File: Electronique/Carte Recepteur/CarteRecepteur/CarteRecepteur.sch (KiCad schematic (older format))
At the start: 1 part

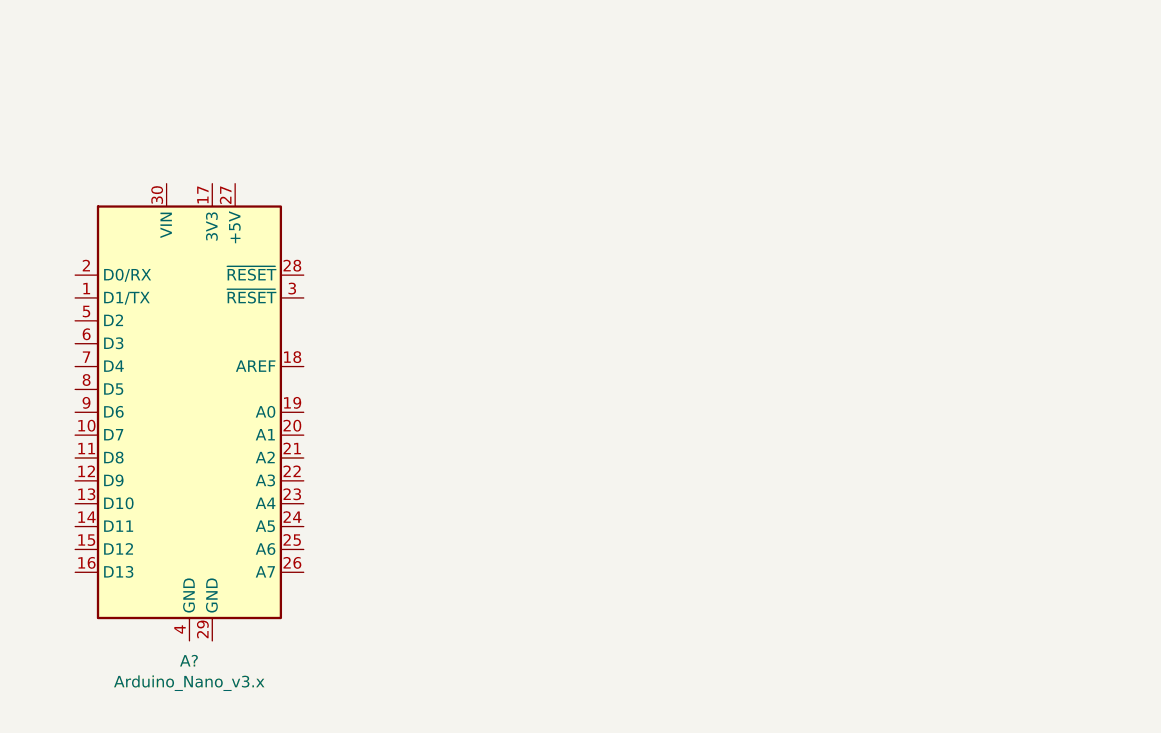
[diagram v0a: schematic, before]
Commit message: ajout trous vis bloc moteurs chassis
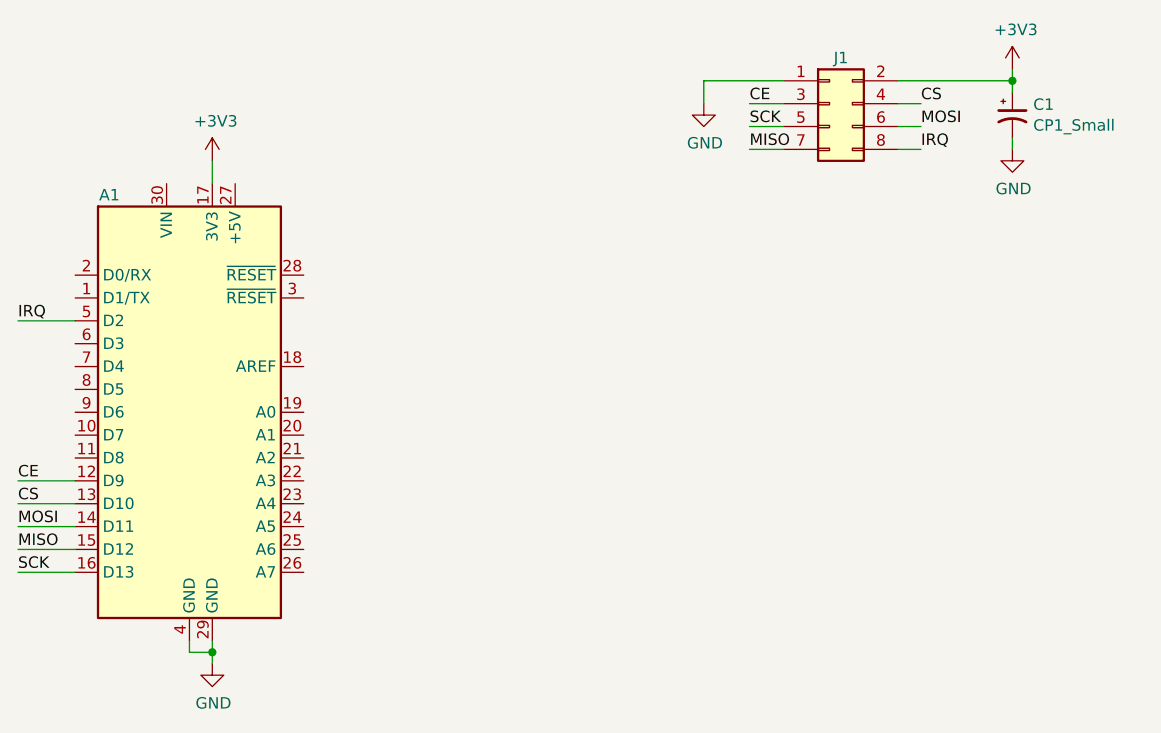
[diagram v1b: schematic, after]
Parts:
- added C1: CP1_Small, Capacitor_THT:CP_Radial_D5.0mm_P2.50mm, symbol Device:CP1_Small
- added J1: Conn_02x04_Odd_Even_MountingPin, Connector_PinHeader_2.54mm:PinHeader_2x04_P2.54mm_Vertical, symbol Connector_Generic:Conn_02x04_Odd_Even
- gave numbers to parts that had none: 1
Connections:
- net CE: now reaches A1.12 (D9)
- net CE: now also J1.3 (Pin_3)
- net CS: now reaches A1.13 (D10)
- net CS: now also J1.4 (Pin_4)
- net MOSI: now reaches A1.14 (D11)
- net MOSI: now also J1.6 (Pin_6)
- net MISO: now reaches A1.15 (D12)
- net MISO: now also J1.7 (Pin_7)
- net SCK: now reaches A1.16 (D13)
- net SCK: now also J1.5 (Pin_5)
- net +3V3: now reaches A1.17 (3V3)
- net +3V3: now also C1.1, J1.2 (Pin_2)
- net GND: now reaches A1.29 (GND)
- net GND: now also A1.4 (GND), C1.2, J1.1 (Pin_1)
- net IRQ: now reaches A1.5 (D2)
- net IRQ: now also J1.8 (Pin_8)
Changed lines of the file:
@@
 $EndDescr
 $Comp
-L MCU_Module:Arduino_Nano_v3.x A?
+L MCU_Module:Arduino_Nano_v3.x A1
 U 1 1 61373980
 P 4050 3000
-F 0 "A?" H 4050 1911 50  0000 C CNN
-F 1 "Arduino_Nano_v3.x" H 4050 1820 50  0000 C CNN
+F 0 "A1" H 3700 3950 50  0000 C CNN
+F 1 "Arduino_Nano_v3.x" H 4050 1820 50  0001 C CNN
 F 2 "Module:Arduino_Nano" H 4050 3000 50  0001 C CIN
 F 3 "http://www.mouser.com/pdfdocs/Gravitech_Arduino_Nano3_0.pdf" H 4050 3000 50  0001 C CNN
@@
 	1    0    0    -1
 $EndComp
+$Comp
+L Connector_Generic:Conn_02x04_Odd_Even J1
+U 1 1 613798DD
+P 6850 1650
+F 0 "J1" H 6900 1850 50  0000 C CNN
+F 1 "Conn_02x04_Odd_Even_MountingPin" H 6900 1300 50  0001 C CNN
+F 2 "Connector_PinHeader_2.54mm:PinHeader_2x04_P2.54mm_Vertical" H 6850 1650 50  0001 C CNN
+F 3 "~" H 6850 1650 50  0001 C CNN
+	1    6850 1650
+	1    0    0    -1
+$EndComp
+$Comp
+L power:+3V3 #PWR0101
+U 1 1 6137ADBA
+P 4150 1900
+F 0 "#PWR0101" H 4150 1750 50  0001 C CNN
+F 1 "+3V3" H 4165 2073 50  0000 C CNN
+F 2 "" H 4150 1900 50  0001 C CNN
+F 3 "" H 4150 1900 50  0001 C CNN
+	1    4150 1900
+	1    0    0    -1
+$EndComp
+Wire Wire Line
+	4150 2000 4150 1900
+$Comp
+L power:+3V3 #PWR0102
+U 1 1 6137B938
+P 7650 1500
+F 0 "#PWR0102" H 7650 1350 50  0001 C CNN
+F 1 "+3V3" H 7665 1673 50  0000 C CNN
+F 2 "" H 7650 1500 50  0001 C CNN
+F 3 "" H 7650 1500 50  0001 C CNN
+	1    7650 1500
+	1    0    0    -1
+$EndComp
+Wire Wire Line
+	7650 1550 7650 1500
+$Comp
+L Device:CP1_Small C1
+U 1 1 6137E190
+P 7650 1700
+F 0 "C1" H 7741 1746 50  0000 L CNN
+F 1 "CP1_Small" H 7741 1655 50  0000 L CNN
+F 2 "Capacitor_THT:CP_Radial_D5.0mm_P2.50mm" H 7650 1700 50  0001 C CNN
+F 3 "~" H 7650 1700 50  0001 C CNN
+	1    7650 1700
+	1    0    0    -1
+$EndComp
+Wire Wire Line
+	7650 1600 7650 1550
+Connection ~ 7650 1550
+$Comp
+L power:GND #PWR0103
+U 1 1 6137E9C8
+P 7650 1850
+F 0 "#PWR0103" H 7650 1600 50  0001 C CNN
+F 1 "GND" H 7655 1677 50  0000 C CNN
+F 2 "" H 7650 1850 50  0001 C CNN
+F 3 "" H 7650 1850 50  0001 C CNN
+	1    7650 1850
+	1    0    0    -1
+$EndComp
+Wire Wire Line
+	7650 1800 7650 1850
+$Comp
+L power:GND #PWR0104
+U 1 1 6137F4C9
+P 4150 4100
+F 0 "#PWR0104" H 4150 3850 50  0001 C CNN
+F 1 "GND" H 4155 3927 50  0000 C CNN
+F 2 "" H 4150 4100 50  0001 C CNN
+F 3 "" H 4150 4100 50  0001 C CNN
+	1    4150 4100
+	1    0    0    -1
+$EndComp
+Wire Wire Line
+	4150 4100 4150 4050
+Wire Wire Line
+	4150 4050 4050 4050
+Wire Wire Line
+	4050 4050 4050 4000
+Connection ~ 4150 4050
+Wire Wire Line
+	4150 4050 4150 4000
+Wire Wire Line
+	7150 1550 7650 1550
+Wire Wire Line
+	7150 1650 7250 1650
+Wire Wire Line
+	7150 1750 7250 1750
+Wire Wire Line
+	7150 1850 7250 1850
+Text Label 7250 1650 0    50   ~ 0
+CS
+Text Label 7250 1750 0    50   ~ 0
+MOSI
+Text Label 7250 1850 0    50   ~ 0
+IRQ
+Text Label 6500 1650 0    50   ~ 0
+CE
+Text Label 6500 1750 0    50   ~ 0
+SCK
+Text Label 6500 1850 0    50   ~ 0
+MISO
+$Comp
+L power:GND #PWR0105
+U 1 1 61381943
+P 6300 1650
+F 0 "#PWR0105" H 6300 1400 50  0001 C CNN
+F 1 "GND" H 6305 1477 50  0000 C CNN
+F 2 "" H 6300 1650 50  0001 C CNN
+F 3 "" H 6300 1650 50  0001 C CNN
+	1    6300 1650
+	1    0    0    -1
+$EndComp
+Wire Wire Line
+	6300 1550 6300 1650
+Wire Wire Line
+	6300 1550 6650 1550
+Wire Wire Line
+	6500 1650 6650 1650
+Wire Wire Line
+	6500 1750 6650 1750
+Wire Wire Line
+	6500 1850 6650 1850
+Wire Wire Line
+	3300 3700 3550 3700
+Text Label 3300 3700 0    50   ~ 0
+SCK
+Wire Wire Line
+	3550 3600 3300 3600
+Wire Wire Line
+	3550 3500 3300 3500
+Wire Wire Line
+	3550 3400 3300 3400
+Text Label 3300 3600 0    50   ~ 0
+MISO
+Text Label 3300 3500 0    50   ~ 0
+MOSI
+Text Label 3300 3400 0    50   ~ 0
+CS
+Wire Wire Line
+	3550 3300 3300 3300
+Text Label 3300 3300 0    50   ~ 0
+CE
+Text Label 3300 2600 0    50   ~ 0
+IRQ
+Wire Wire Line
+	3300 2600 3550 2600
 $EndSCHEMATC

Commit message: pcb recepteur
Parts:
- added H1, H2: MountingHole, MountingHole:MountingHole_2.2mm_M2_ISO7380_Pad, symbol Mechanical:MountingHole
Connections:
- net CE: now also A1.23 (A4); no longer A1.12 (D9)
- net IRQ: no longer A1.5 (D2)
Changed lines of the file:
@@
 $EndDescr
-$Comp
-L MCU_Module:Arduino_Nano_v3.x A1
-U 1 1 61373980
-P 4050 3000
-F 0 "A1" H 3700 3950 50  0000 C CNN
-F 1 "Arduino_Nano_v3.x" H 4050 1820 50  0001 C CNN
-F 2 "Module:Arduino_Nano" H 4050 3000 50  0001 C CIN
-F 3 "http://www.mouser.com/pdfdocs/Gravitech_Arduino_Nano3_0.pdf" H 4050 3000 50  0001 C CNN
-	1    4050 3000
-	1    0    0    -1
-$EndComp
 $Comp
 L Connector_Generic:Conn_02x04_Odd_Even J1
@@
 Text Label 3300 3400 0    50   ~ 0
 CS
+$Comp
+L Mechanical:MountingHole H1
+U 1 1 613A0057
+P 6250 2850
+F 0 "H1" H 6350 2896 50  0000 L CNN
+F 1 "MountingHole" H 6350 2805 50  0000 L CNN
+F 2 "MountingHole:MountingHole_2.2mm_M2_ISO7380_Pad" H 6250 2850 50  0001 C CNN
+F 3 "~" H 6250 2850 50  0001 C CNN
+	1    6250 2850
+	1    0    0    -1
+$EndComp
+$Comp
+L Mechanical:MountingHole H2
+U 1 1 613A4CAC
+P 6250 3050
+F 0 "H2" H 6350 3096 50  0000 L CNN
+F 1 "MountingHole" H 6350 3005 50  0000 L CNN
+F 2 "MountingHole:MountingHole_2.2mm_M2_ISO7380_Pad" H 6250 3050 50  0001 C CNN
+F 3 "~" H 6250 3050 50  0001 C CNN
+	1    6250 3050
+	1    0    0    -1
+$EndComp
+Text Label 4700 3400 0    50   ~ 0
+CE
 Wire Wire Line
-	3550 3300 3300 3300
-Text Label 3300 3300 0    50   ~ 0
-CE
-Text Label 3300 2600 0    50   ~ 0
-IRQ
-Wire Wire Line
-	3300 2600 3550 2600
+	4550 3400 4700 3400
+$Comp
+L MCU_Module:Arduino_Nano_v3.x A1
+U 1 1 61373980
+P 4050 3000
+F 0 "A1" H 3700 3950 50  0000 C CNN
+F 1 "Arduino_Nano_v3.x" H 4050 1820 50  0001 C CNN
+F 2 "Module:Arduino_Nano" H 4050 3000 50  0001 C CIN
+F 3 "http://www.mouser.com/pdfdocs/Gravitech_Arduino_Nano3_0.pdf" H 4050 3000 50  0001 C CNN
+	1    4050 3000
+	1    0    0    -1
+$EndComp
 $EndSCHEMATC
